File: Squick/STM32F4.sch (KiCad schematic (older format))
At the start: 30 parts, among them J1 BT, J2 DEBUG_UART, J3 PROG, SW1 USER_BUT_1, SW2 USER_BUT_2, SW3 RESET, U1 STM32F411RETx

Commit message: Fixed footprints and symbol
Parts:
- SW1, SW2, SW3: footprint Button_Switch_SMD:Tact_Switch_SMD_3x6mm -> Button_Switch_SMD:SW_DIP_SPSTx01_Slide_6.7x4.1mm_W6.73mm_P2.54mm_LowProfile_JPin
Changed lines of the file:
@@
 F 0 "SW3" H 5750 2385 50  0000 C CNN
 F 1 "RESET" H 5750 2294 50  0000 C CNN
-F 2 "Button_Switch_SMD:Tact_Switch_SMD_3x6mm" H 5750 2300 50  0001 C CNN
+F 2 "Button_Switch_SMD:SW_DIP_SPSTx01_Slide_6.7x4.1mm_W6.73mm_P2.54mm_LowProfile_JPin" H 5750 2300 50  0001 C CNN
 F 3 "~" H 5750 2300 50  0001 C CNN
 	1    5750 2100
@@
 F 0 "SW1" H 1275 2110 50  0000 C CNN
 F 1 "USER_BUT_1" H 1275 2019 50  0000 C CNN
-F 2 "Button_Switch_SMD:Tact_Switch_SMD_3x6mm" H 1275 2025 50  0001 C CNN
+F 2 "Button_Switch_SMD:SW_DIP_SPSTx01_Slide_6.7x4.1mm_W6.73mm_P2.54mm_LowProfile_JPin" H 1275 2025 50  0001 C CNN
 F 3 "~" H 1275 2025 50  0001 C CNN
 	1    1275 1825
@@
 F 0 "SW2" H 2775 2110 50  0000 C CNN
 F 1 "USER_BUT_2" H 2775 2019 50  0000 C CNN
-F 2 "Button_Switch_SMD:Tact_Switch_SMD_3x6mm" H 2775 2025 50  0001 C CNN
+F 2 "Button_Switch_SMD:SW_DIP_SPSTx01_Slide_6.7x4.1mm_W6.73mm_P2.54mm_LowProfile_JPin" H 2775 2025 50  0001 C CNN
 F 3 "~" H 2775 2025 50  0001 C CNN
 	1    2775 1825

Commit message: Progress with PCB and some footprint debugs
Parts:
- C1, C10, C11, C12, C13, C2, C3, C4, C5, C6, C7, C8, C9: footprint Capacitor_SMD:C_0805_2012Metric -> Capacitor_SMD:C_0603_1608Metric
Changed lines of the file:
@@
 F 0 "C13" V 7750 2250 50  0000 L CNN
 F 1 "4.7u" V 7825 2225 50  0000 L CNN
-F 2 "Capacitor_SMD:C_0805_2012Metric" H 7600 2300 50  0001 C CNN
+F 2 "Capacitor_SMD:C_0603_1608Metric" H 7600 2300 50  0001 C CNN
 F 3 "~" H 7600 2300 50  0001 C CNN
 	1    7600 2300
@@
 F 0 "C8" V 5675 2125 50  0000 L CNN
 F 1 "100n" V 5875 2200 50  0000 L CNN
-F 2 "Capacitor_SMD:C_0805_2012Metric" H 5750 2275 50  0001 C CNN
+F 2 "Capacitor_SMD:C_0603_1608Metric" H 5750 2275 50  0001 C CNN
 F 3 "~" H 5750 2275 50  0001 C CNN
 	1    5750 2275
@@
 F 0 "C3" H 4800 4650 50  0000 L CNN
 F 1 "100n" H 4700 4500 50  0000 L CNN
-F 2 "Capacitor_SMD:C_0805_2012Metric" H 4925 4575 50  0001 C CNN
+F 2 "Capacitor_SMD:C_0603_1608Metric" H 4925 4575 50  0001 C CNN
 F 3 "~" H 4925 4575 50  0001 C CNN
 	1    4925 4575
@@
 F 0 "C4" H 5050 4650 50  0000 L CNN
 F 1 "100n" H 4950 4500 50  0000 L CNN
-F 2 "Capacitor_SMD:C_0805_2012Metric" H 5175 4575 50  0001 C CNN
+F 2 "Capacitor_SMD:C_0603_1608Metric" H 5175 4575 50  0001 C CNN
 F 3 "~" H 5175 4575 50  0001 C CNN
 	1    5175 4575
@@
 F 0 "C5" H 5300 4650 50  0000 L CNN
 F 1 "100n" H 5200 4500 50  0000 L CNN
-F 2 "Capacitor_SMD:C_0805_2012Metric" H 5425 4575 50  0001 C CNN
+F 2 "Capacitor_SMD:C_0603_1608Metric" H 5425 4575 50  0001 C CNN
 F 3 "~" H 5425 4575 50  0001 C CNN
 	1    5425 4575
@@
 F 0 "C6" H 5550 4650 50  0000 L CNN
 F 1 "100n" H 5450 4500 50  0000 L CNN
-F 2 "Capacitor_SMD:C_0805_2012Metric" H 5675 4575 50  0001 C CNN
+F 2 "Capacitor_SMD:C_0603_1608Metric" H 5675 4575 50  0001 C CNN
 F 3 "~" H 5675 4575 50  0001 C CNN
 	1    5675 4575
@@
 F 0 "C12" H 6450 4500 50  0000 L CNN
 F 1 "4.7u" H 6450 4650 50  0000 L CNN
-F 2 "Capacitor_SMD:C_0805_2012Metric" H 6425 4575 50  0001 C CNN
+F 2 "Capacitor_SMD:C_0603_1608Metric" H 6425 4575 50  0001 C CNN
 F 3 "~" H 6425 4575 50  0001 C CNN
 	1    6425 4575
@@
 F 0 "C9" H 5800 4650 50  0000 L CNN
 F 1 "100n" H 5700 4500 50  0000 L CNN
-F 2 "Capacitor_SMD:C_0805_2012Metric" H 5925 4575 50  0001 C CNN
+F 2 "Capacitor_SMD:C_0603_1608Metric" H 5925 4575 50  0001 C CNN
 F 3 "~" H 5925 4575 50  0001 C CNN
 	1    5925 4575
@@
 F 0 "C11" H 6050 4650 50  0000 L CNN
 F 1 "100n" H 5950 4500 50  0000 L CNN
-F 2 "Capacitor_SMD:C_0805_2012Metric" H 6175 4575 50  0001 C CNN
+F 2 "Capacitor_SMD:C_0603_1608Metric" H 6175 4575 50  0001 C CNN
 F 3 "~" H 6175 4575 50  0001 C CNN
 	1    6175 4575
@@
 F 0 "C10" H 5850 3450 50  0000 L CNN
 F 1 "1u" H 5850 3600 50  0000 L CNN
-F 2 "Capacitor_SMD:C_0805_2012Metric" H 6000 3525 50  0001 C CNN
+F 2 "Capacitor_SMD:C_0603_1608Metric" H 6000 3525 50  0001 C CNN
 F 3 "~" H 6000 3525 50  0001 C CNN
 	1    6000 3525
@@
 F 0 "C7" H 5550 3450 50  0000 L CNN
 F 1 "100n" H 5500 3600 50  0000 L CNN
-F 2 "Capacitor_SMD:C_0805_2012Metric" H 5700 3525 50  0001 C CNN
+F 2 "Capacitor_SMD:C_0603_1608Metric" H 5700 3525 50  0001 C CNN
 F 3 "~" H 5700 3525 50  0001 C CNN
 	1    5700 3525
@@
 F 0 "C1" V 1200 1850 50  0000 L CNN
 F 1 "100n" V 1400 1925 50  0000 L CNN
-F 2 "Capacitor_SMD:C_0805_2012Metric" H 1275 2000 50  0001 C CNN
+F 2 "Capacitor_SMD:C_0603_1608Metric" H 1275 2000 50  0001 C CNN
 F 3 "~" H 1275 2000 50  0001 C CNN
 	1    1275 2000
@@
 F 0 "C2" V 2700 1850 50  0000 L CNN
 F 1 "100n" V 2900 1925 50  0000 L CNN
-F 2 "Capacitor_SMD:C_0805_2012Metric" H 2775 2000 50  0001 C CNN
+F 2 "Capacitor_SMD:C_0603_1608Metric" H 2775 2000 50  0001 C CNN
 F 3 "~" H 2775 2000 50  0001 C CNN
 	1    2775 2000

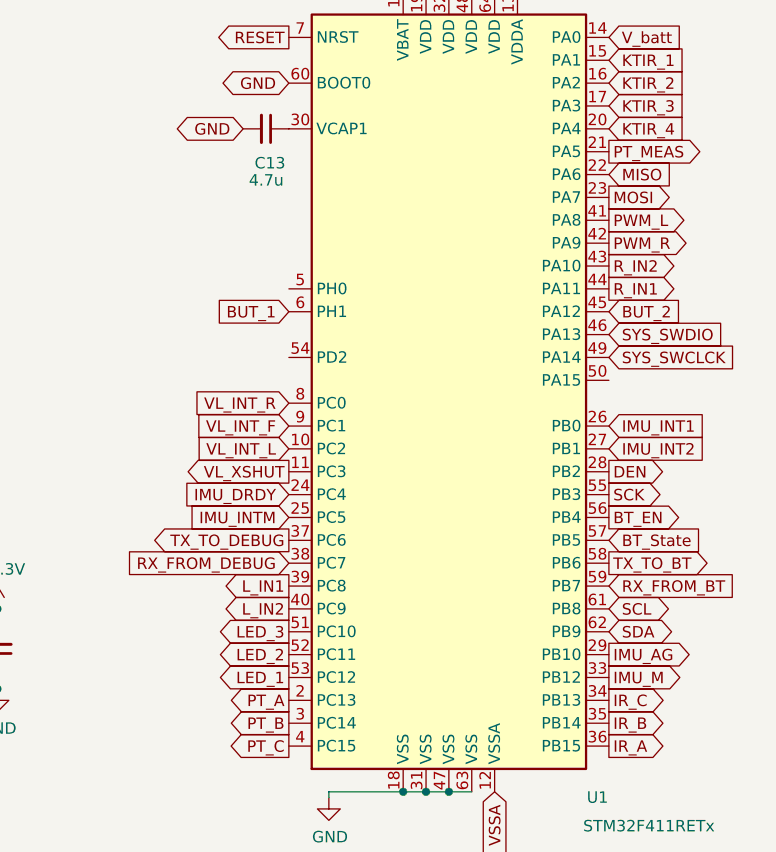
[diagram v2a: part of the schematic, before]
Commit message: Changed IMU and assigned 0603 footprints
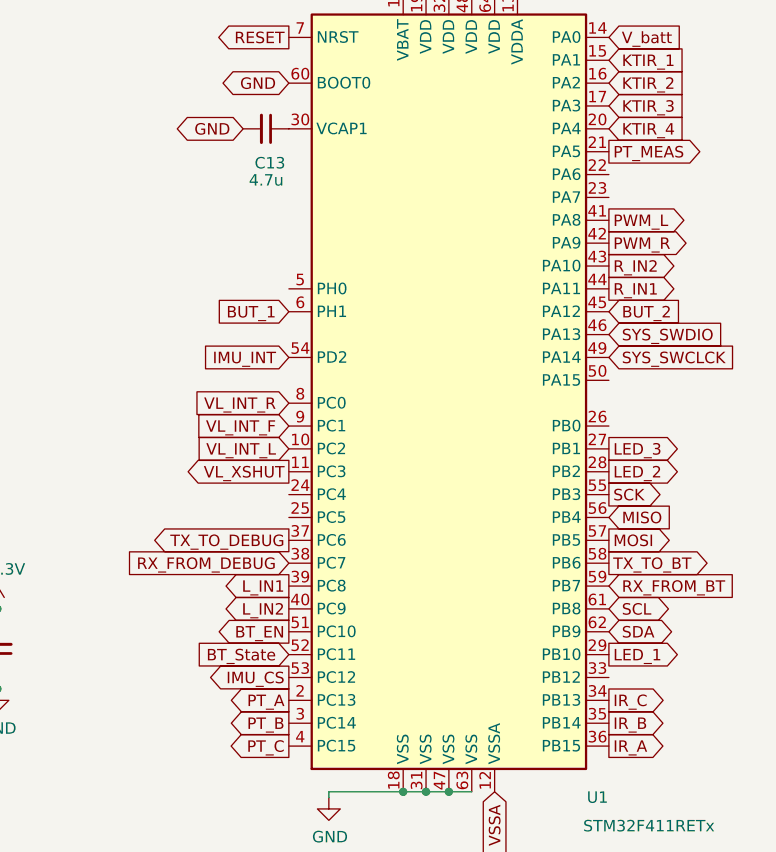
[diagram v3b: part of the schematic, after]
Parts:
- C1, C10, C11, C12, C13, C2, C3, C4, C5, C6, C7, C8, C9: footprint Capacitor_SMD:C_0603_1608Metric -> Capacitor_SMD:C_0603_1608Metric_Pad1.05x0.95mm_HandSolder
- D1, D2, D3: footprint LED_SMD:LED_0805_2012Metric -> LED_SMD:LED_0603_1608Metric_Pad1.05x0.95mm_HandSolder
- L1: footprint Inductor_SMD:L_0805_2012Metric -> Inductor_SMD:L_0603_1608Metric_Pad1.05x0.95mm_HandSolder
- R1, R2, R3, R4, R5, R6: footprint Resistor_SMD:R_0805_2012Metric -> Resistor_SMD:R_0603_1608Metric_Pad1.05x0.95mm_HandSolder
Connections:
- net DEN is gone; now on net LED_2: U1.28 (PB2)
- net IMU_AG is gone; now on net LED_1: U1.29 (PB10)
- net IMU_INT2 is gone; now on net LED_3: U1.27 (PB1)
- net BT_EN: now also U1.51 (PC10); no longer U1.56 (PB4)
- net BT_State: now also U1.52 (PC11); no longer U1.57 (PB5)
- net LED_1: no longer U1.53 (PC12)
- net LED_2: no longer U1.52 (PC11)
- net LED_3: no longer U1.51 (PC10)
- net MISO: now also U1.56 (PB4); no longer U1.22 (PA6)
- net MOSI: now also U1.57 (PB5); no longer U1.23 (PA7)
- net IMU_INT: now reaches U1.54 (PD2)
- net IMU_DRDY: no longer names the net of U1.24 (PC4)
- net IMU_INT1: no longer names the net of U1.26 (PB0)
- net IMU_INTM: no longer names the net of U1.25 (PC5)
- net IMU_M: no longer names the net of U1.33 (PB12)
- new net IMU_CS: U1.53 (PC12)
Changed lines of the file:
@@
 EESchema Schematic File Version 4
-LIBS:Squick-cache
-EELAYER 26 0
+EELAYER 30 0
 EELAYER END
 $Descr A4 11693 8268
@@
 F 0 "C13" V 7750 2250 50  0000 L CNN
 F 1 "4.7u" V 7825 2225 50  0000 L CNN
-F 2 "Capacitor_SMD:C_0603_1608Metric" H 7600 2300 50  0001 C CNN
+F 2 "Capacitor_SMD:C_0603_1608Metric_Pad1.05x0.95mm_HandSolder" H 7600 2300 50  0001 C CNN
 F 3 "~" H 7600 2300 50  0001 C CNN
 	1    7600 2300
@@
 F 0 "C8" V 5675 2125 50  0000 L CNN
 F 1 "100n" V 5875 2200 50  0000 L CNN
-F 2 "Capacitor_SMD:C_0603_1608Metric" H 5750 2275 50  0001 C CNN
+F 2 "Capacitor_SMD:C_0603_1608Metric_Pad1.05x0.95mm_HandSolder" H 5750 2275 50  0001 C CNN
 F 3 "~" H 5750 2275 50  0001 C CNN
 	1    5750 2275
@@
 F 0 "C3" H 4800 4650 50  0000 L CNN
 F 1 "100n" H 4700 4500 50  0000 L CNN
-F 2 "Capacitor_SMD:C_0603_1608Metric" H 4925 4575 50  0001 C CNN
+F 2 "Capacitor_SMD:C_0603_1608Metric_Pad1.05x0.95mm_HandSolder" H 4925 4575 50  0001 C CNN
 F 3 "~" H 4925 4575 50  0001 C CNN
 	1    4925 4575
@@
 F 0 "C4" H 5050 4650 50  0000 L CNN
 F 1 "100n" H 4950 4500 50  0000 L CNN
-F 2 "Capacitor_SMD:C_0603_1608Metric" H 5175 4575 50  0001 C CNN
+F 2 "Capacitor_SMD:C_0603_1608Metric_Pad1.05x0.95mm_HandSolder" H 5175 4575 50  0001 C CNN
 F 3 "~" H 5175 4575 50  0001 C CNN
 	1    5175 4575
@@
 F 0 "C5" H 5300 4650 50  0000 L CNN
 F 1 "100n" H 5200 4500 50  0000 L CNN
-F 2 "Capacitor_SMD:C_0603_1608Metric" H 5425 4575 50  0001 C CNN
+F 2 "Capacitor_SMD:C_0603_1608Metric_Pad1.05x0.95mm_HandSolder" H 5425 4575 50  0001 C CNN
 F 3 "~" H 5425 4575 50  0001 C CNN
 	1    5425 4575
@@
 F 0 "C6" H 5550 4650 50  0000 L CNN
 F 1 "100n" H 5450 4500 50  0000 L CNN
-F 2 "Capacitor_SMD:C_0603_1608Metric" H 5675 4575 50  0001 C CNN
+F 2 "Capacitor_SMD:C_0603_1608Metric_Pad1.05x0.95mm_HandSolder" H 5675 4575 50  0001 C CNN
 F 3 "~" H 5675 4575 50  0001 C CNN
 	1    5675 4575
@@
 F 0 "C12" H 6450 4500 50  0000 L CNN
 F 1 "4.7u" H 6450 4650 50  0000 L CNN
-F 2 "Capacitor_SMD:C_0603_1608Metric" H 6425 4575 50  0001 C CNN
+F 2 "Capacitor_SMD:C_0603_1608Metric_Pad1.05x0.95mm_HandSolder" H 6425 4575 50  0001 C CNN
 F 3 "~" H 6425 4575 50  0001 C CNN
 	1    6425 4575
@@
 F 0 "C9" H 5800 4650 50  0000 L CNN
 F 1 "100n" H 5700 4500 50  0000 L CNN
-F 2 "Capacitor_SMD:C_0603_1608Metric" H 5925 4575 50  0001 C CNN
+F 2 "Capacitor_SMD:C_0603_1608Metric_Pad1.05x0.95mm_HandSolder" H 5925 4575 50  0001 C CNN
 F 3 "~" H 5925 4575 50  0001 C CNN
 	1    5925 4575
@@
 F 0 "C11" H 6050 4650 50  0000 L CNN
 F 1 "100n" H 5950 4500 50  0000 L CNN
-F 2 "Capacitor_SMD:C_0603_1608Metric" H 6175 4575 50  0001 C CNN
+F 2 "Capacitor_SMD:C_0603_1608Metric_Pad1.05x0.95mm_HandSolder" H 6175 4575 50  0001 C CNN
 F 3 "~" H 6175 4575 50  0001 C CNN
 	1    6175 4575
@@
 F 0 "C10" H 5850 3450 50  0000 L CNN
 F 1 "1u" H 5850 3600 50  0000 L CNN
-F 2 "Capacitor_SMD:C_0603_1608Metric" H 6000 3525 50  0001 C CNN
+F 2 "Capacitor_SMD:C_0603_1608Metric_Pad1.05x0.95mm_HandSolder" H 6000 3525 50  0001 C CNN
 F 3 "~" H 6000 3525 50  0001 C CNN
 	1    6000 3525
@@
 F 0 "C7" H 5550 3450 50  0000 L CNN
 F 1 "100n" H 5500 3600 50  0000 L CNN
-F 2 "Capacitor_SMD:C_0603_1608Metric" H 5700 3525 50  0001 C CNN
+F 2 "Capacitor_SMD:C_0603_1608Metric_Pad1.05x0.95mm_HandSolder" H 5700 3525 50  0001 C CNN
 F 3 "~" H 5700 3525 50  0001 C CNN
 	1    5700 3525
@@
 F 0 "L1" V 5244 3350 50  0000 C CNN
 F 1 "10u" V 5335 3350 50  0000 C CNN
-F 2 "Inductor_SMD:L_0805_2012Metric" H 5425 3350 50  0001 C CNN
+F 2 "Inductor_SMD:L_0603_1608Metric_Pad1.05x0.95mm_HandSolder" H 5425 3350 50  0001 C CNN
 F 3 "~" H 5425 3350 50  0001 C CNN
 	1    5425 3350
@@
 F 0 "R6" H 6000 2050 50  0000 L CNN
 F 1 "100k" H 6000 1950 50  0000 L CNN
-F 2 "Resistor_SMD:R_0805_2012Metric" H 5950 1950 50  0001 C CNN
+F 2 "Resistor_SMD:R_0603_1608Metric_Pad1.05x0.95mm_HandSolder" H 5950 1950 50  0001 C CNN
 F 3 "~" H 5950 1950 50  0001 C CNN
 	1    5950 1950
@@
 Wire Wire Line
 	5950 2050 5950 2100
-Text GLabel 7700 3900 0    50   Input ~ 0
-IMU_DRDY
-Text GLabel 7700 4000 0    50   Input ~ 0
-IMU_INTM
 Connection ~ 8200 5200
 Connection ~ 8300 5200
@@
 Wire Wire Line
 	8400 1700 8300 1700
-Text GLabel 9100 3800 2    50   Output ~ 0
-DEN
-Text GLabel 9100 3700 2    50   Input ~ 0
-IMU_INT2
-Text GLabel 9100 3600 2    50   Input ~ 0
-IMU_INT1
-Text GLabel 9100 2600 2    50   Output ~ 0
-MOSI
-Text GLabel 9100 2500 2    50   Input ~ 0
+Text GLabel 7700 4700 0    50   Output ~ 0
+IMU_CS
+Text GLabel 7700 3300 0    50   Input ~ 0
+IMU_INT
+Text GLabel 9100 4000 2    50   Input ~ 0
 MISO
 Text GLabel 9100 3900 2    50   Output ~ 0
@@
 Text Notes 7325 1375 0    100  ~ 0
 Microcontroler STM32
-Text GLabel 9100 4600 2    50   Output ~ 0
-IMU_AG
-Text GLabel 9100 4700 2    50   Output ~ 0
-IMU_M
-Text GLabel 9100 4100 2    50   Input ~ 0
+Text GLabel 7700 4600 0    50   Input ~ 0
 BT_State
-Text GLabel 9100 4000 2    50   Output ~ 0
+Text GLabel 7700 4500 0    50   Output ~ 0
 BT_EN
 Text GLabel 9100 4800 2    50   Output ~ 0
@@
 F 0 "C1" V 1200 1850 50  0000 L CNN
 F 1 "100n" V 1400 1925 50  0000 L CNN
-F 2 "Capacitor_SMD:C_0603_1608Metric" H 1275 2000 50  0001 C CNN
+F 2 "Capacitor_SMD:C_0603_1608Metric_Pad1.05x0.95mm_HandSolder" H 1275 2000 50  0001 C CNN
 F 3 "~" H 1275 2000 50  0001 C CNN
 	1    1275 2000
@@
 F 0 "R1" H 1700 1775 50  0000 L CNN
 F 1 "100k" H 1700 1675 50  0000 L CNN
-F 2 "Resistor_SMD:R_0805_2012Metric" H 1650 1675 50  0001 C CNN
+F 2 "Resistor_SMD:R_0603_1608Metric_Pad1.05x0.95mm_HandSolder" H 1650 1675 50  0001 C CNN
 F 3 "~" H 1650 1675 50  0001 C CNN
 	1    1650 1675
@@
 F 0 "C2" V 2700 1850 50  0000 L CNN
 F 1 "100n" V 2900 1925 50  0000 L CNN
-F 2 "Capacitor_SMD:C_0603_1608Metric" H 2775 2000 50  0001 C CNN
+F 2 "Capacitor_SMD:C_0603_1608Metric_Pad1.05x0.95mm_HandSolder" H 2775 2000 50  0001 C CNN
 F 3 "~" H 2775 2000 50  0001 C CNN
 	1    2775 2000
@@
 F 0 "R5" H 3200 1775 50  0000 L CNN
 F 1 "100k" H 3200 1675 50  0000 L CNN
-F 2 "Resistor_SMD:R_0805_2012Metric" H 3150 1675 50  0001 C CNN
+F 2 "Resistor_SMD:R_0603_1608Metric_Pad1.05x0.95mm_HandSolder" H 3150 1675 50  0001 C CNN
 F 3 "~" H 3150 1675 50  0001 C CNN
 	1    3150 1675
@@
 F 0 "D1" H 1425 3250 50  0000 C CNN
 F 1 "LED_1" H 1425 3550 50  0000 C CNN
-F 2 "LED_SMD:LED_0805_2012Metric" H 1425 3425 50  0001 C CNN
+F 2 "LED_SMD:LED_0603_1608Metric_Pad1.05x0.95mm_HandSolder" H 1425 3425 50  0001 C CNN
 F 3 "~" H 1425 3425 50  0001 C CNN
 	1    1425 3425
@@
 F 0 "R2" V 1543 3425 50  0000 C CNN
 F 1 "220" V 1634 3425 50  0000 C CNN
-F 2 "Resistor_SMD:R_0805_2012Metric" V 1680 3425 50  0001 C CNN
+F 2 "Resistor_SMD:R_0603_1608Metric_Pad1.05x0.95mm_HandSolder" V 1680 3425 50  0001 C CNN
 F 3 "~" H 1750 3425 50  0001 C CNN
 	1    1750 3425
@@
 F 0 "D2" H 1450 3850 50  0000 C CNN
 F 1 "LED_2" H 1450 4150 50  0000 C CNN
-F 2 "LED_SMD:LED_0805_2012Metric" H 1450 4025 50  0001 C CNN
+F 2 "LED_SMD:LED_0603_1608Metric_Pad1.05x0.95mm_HandSolder" H 1450 4025 50  0001 C CNN
 F 3 "~" H 1450 4025 50  0001 C CNN
 	1    1450 4025
@@
 F 0 "R3" V 1568 4025 50  0000 C CNN
 F 1 "220" V 1659 4025 50  0000 C CNN
-F 2 "Resistor_SMD:R_0805_2012Metric" V 1705 4025 50  0001 C CNN
+F 2 "Resistor_SMD:R_0603_1608Metric_Pad1.05x0.95mm_HandSolder" V 1705 4025 50  0001 C CNN
 F 3 "~" H 1775 4025 50  0001 C CNN
 	1    1775 4025
@@
 F 0 "D3" H 1475 4500 50  0000 C CNN
 F 1 "LED_3" H 1475 4800 50  0000 C CNN
-F 2 "LED_SMD:LED_0805_2012Metric" H 1475 4675 50  0001 C CNN
+F 2 "LED_SMD:LED_0603_1608Metric_Pad1.05x0.95mm_HandSolder" H 1475 4675 50  0001 C CNN
 F 3 "~" H 1475 4675 50  0001 C CNN
 	1    1475 4675
@@
 F 0 "R4" V 1593 4675 50  0000 C CNN
 F 1 "220" V 1684 4675 50  0000 C CNN
-F 2 "Resistor_SMD:R_0805_2012Metric" V 1730 4675 50  0001 C CNN
+F 2 "Resistor_SMD:R_0603_1608Metric_Pad1.05x0.95mm_HandSolder" V 1730 4675 50  0001 C CNN
 F 3 "~" H 1800 4675 50  0001 C CNN
 	1    1800 4675
@@
 Text GLabel 2025 4675 2    50   Output ~ 0
 LED_3
-Text GLabel 7700 4700 0    50   Output ~ 0
+Text GLabel 9100 4600 2    50   Output ~ 0
 LED_1
-Text GLabel 7700 4600 0    50   Output ~ 0
+Text GLabel 9100 3800 2    50   Output ~ 0
 LED_2
-Text GLabel 7700 4500 0    50   Output ~ 0
+Text GLabel 9100 3700 2    50   Output ~ 0
 LED_3
+Text GLabel 9100 4100 2    50   Output ~ 0
+MOSI
 $EndSCHEMATC

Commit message: some debugs and small changes
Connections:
- no-connect marks 0 -> 8
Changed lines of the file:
@@
 EESchema Schematic File Version 4
-EELAYER 30 0
+LIBS:Squick-cache
+EELAYER 26 0
 EELAYER END
 $Descr A4 11693 8268
@@
 Text GLabel 9100 4100 2    50   Output ~ 0
 MOSI
+NoConn ~ 9100 4700
+NoConn ~ 9100 3600
+NoConn ~ 9100 3400
+NoConn ~ 9100 2600
+NoConn ~ 9100 2500
+NoConn ~ 7700 3000
+NoConn ~ 7700 3900
+NoConn ~ 7700 4000
 $EndSCHEMATC
